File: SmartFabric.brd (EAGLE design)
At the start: 160 x 100 mm, 1 part

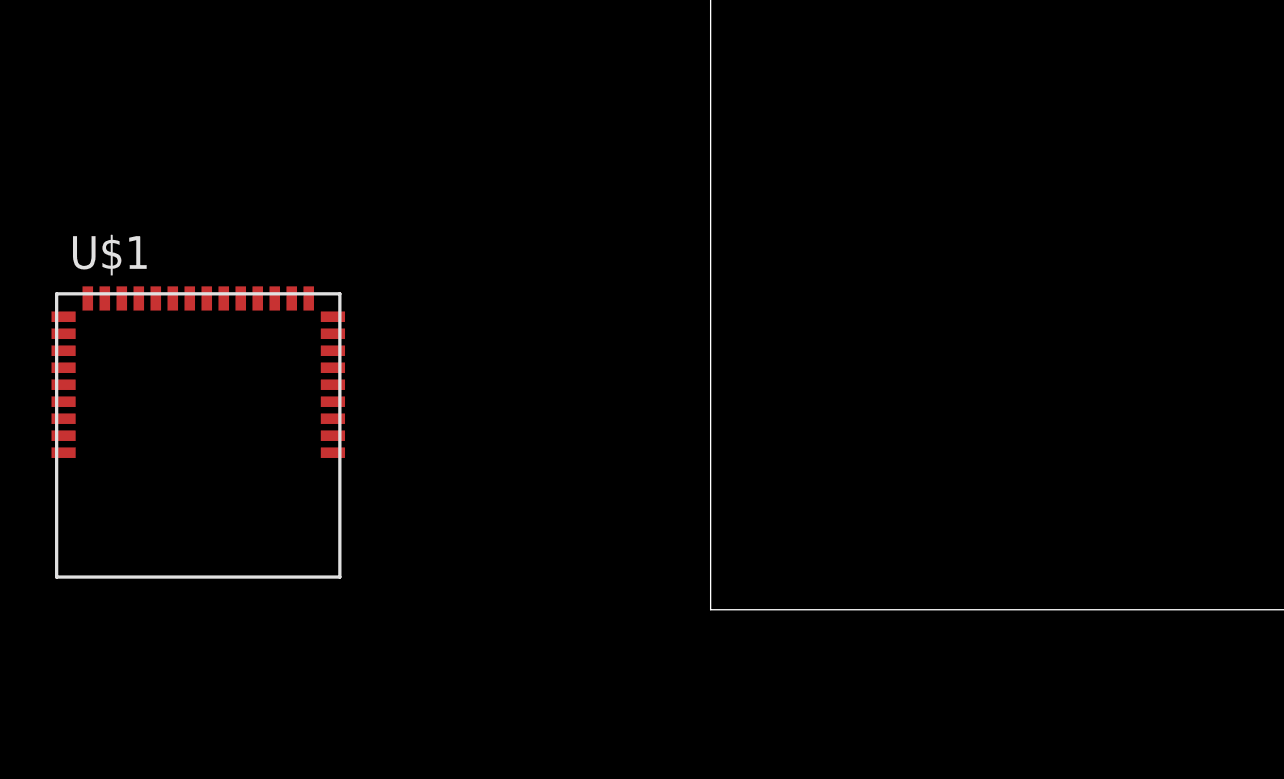
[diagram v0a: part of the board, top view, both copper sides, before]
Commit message: added gitignore and wired power and added a ferrite bead
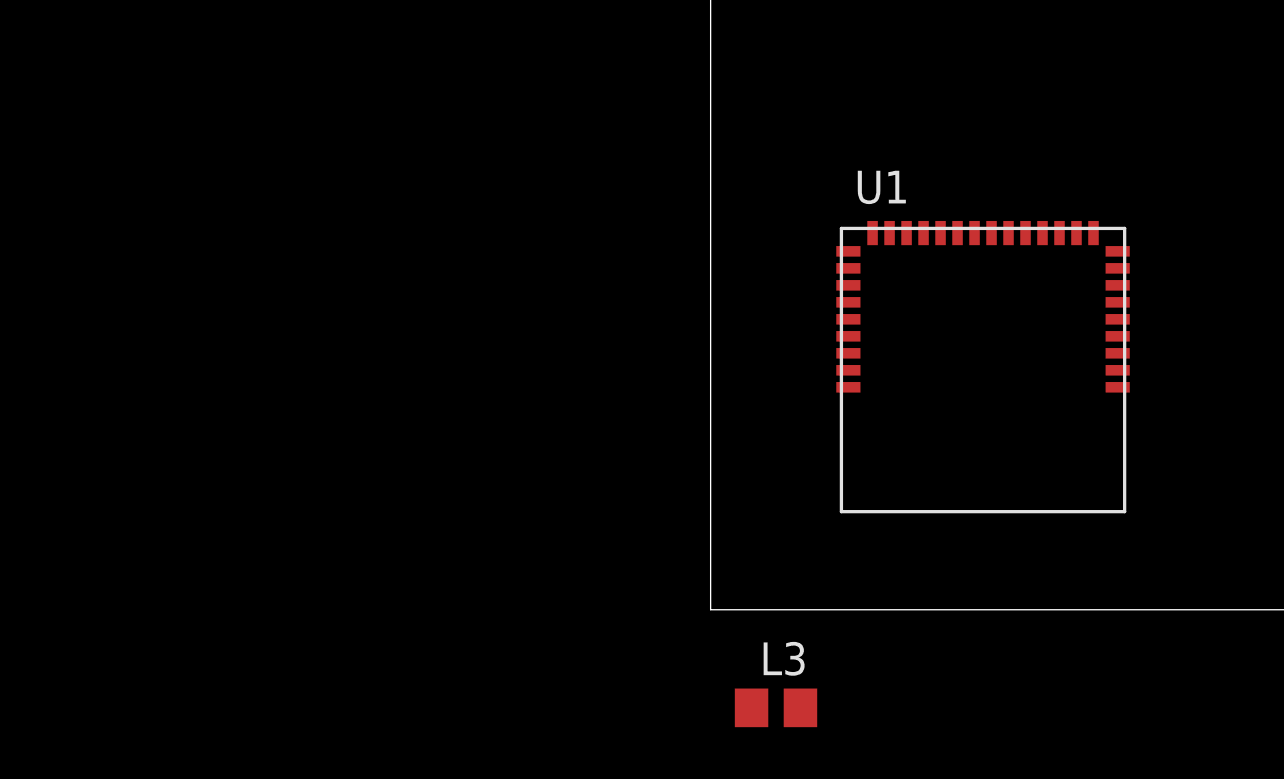
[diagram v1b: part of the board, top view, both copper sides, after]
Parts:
- removed U$1: CYPRESS-EZ-BLE-PSOC, wicked-device:CYPRESS-EZ-BLE-PROC
- added L3: FERRITE, rcl:R0805
- added U1: CYPRESS-EZ-BLE-PSOC, wicked-device:CYPRESS-EZ-BLE-PROC
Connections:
- new net GND: U1.1, U1.32
- new net N$1: L3.1, U1.13, U1.20, U1.7
- new net VCC: L3.2
- new net VREF: U1.26
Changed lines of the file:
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@@
 <layer number="113" name="IDFDebug" color="4" fill="1" visible="yes" active="yes"/>
 <layer number="116" name="Patch_BOT" color="9" fill="4" visible="yes" active="yes"/>
+<layer number="118" name="Rect_Pads" color="7" fill="1" visible="no" active="yes"/>
 <layer number="121" name="_tsilk" color="7" fill="1" visible="yes" active="yes"/>
 <layer number="122" name="_bsilk" color="7" fill="1" visible="yes" active="yes"/>
@@
 <layer number="223" name="223bmp" color="24" fill="1" visible="no" active="no"/>
 <layer number="224" name="224bmp" color="25" fill="1" visible="no" active="no"/>
+<layer number="231" name="Eagle3D_PG1" color="7" fill="1" visible="yes" active="yes"/>
+<layer number="232" name="Eagle3D_PG2" color="7" fill="1" visible="yes" active="yes"/>
+<layer number="233" name="Eagle3D_PG3" color="7" fill="1" visible="yes" active="yes"/>
 <layer number="248" name="Housing" color="7" fill="1" visible="yes" active="yes"/>
 <layer number="249" name="Edge" color="7" fill="1" visible="yes" active="yes"/>
@@
 </autorouter>
 <elements>
-<element name="U$1" library="wicked-device" package="CYPRESS-EZ-BLE-PROC" value="CYPRESS-EZ-BLE-PSOC" x="-25.4" y="1.27"/>
+<element name="U1" library="wicked-device" package="CYPRESS-EZ-BLE-PROC" value="CYPRESS-EZ-BLE-PSOC" x="5.08" y="3.81"/>
+<element name="L3" library="rcl" package="R0805" value="FERRITE" x="2.54" y="-3.81"/>
 </elements>
 <signals>
+<signal name="GND">
+<contactref element="U1" pad="1"/>
+<contactref element="U1" pad="32"/>
+<wire x1="5.35" y1="8.64" x2="15.81" y2="8.64" width="0" layer="19" extent="1-1"/>
+</signal>
+<signal name="N$1">
+<contactref element="U1" pad="20"/>
+<contactref element="L3" pad="1"/>
+<contactref element="U1" pad="13"/>
+<contactref element="U1" pad="7"/>
+<wire x1="15.81" y1="12.6" x2="12.89" y2="14.63" width="0" layer="19" extent="1-1"/>
+<wire x1="8.27" y1="14.63" x2="12.89" y2="14.63" width="0" layer="19" extent="1-1"/>
+<wire x1="1.59" y1="-3.81" x2="8.27" y2="14.63" width="0" layer="19" extent="1-1"/>
+</signal>
+<signal name="VCC">
+<contactref element="L3" pad="2"/>
+</signal>
+<signal name="VREF">
+<contactref element="U1" pad="26"/>
+</signal>
 </signals>
 </board>
